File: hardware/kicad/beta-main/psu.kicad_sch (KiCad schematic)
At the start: 34 parts, among them J18 XT60, U5 AP3441SHE-7B, U6 TPS56624x, U7 AP2553W6

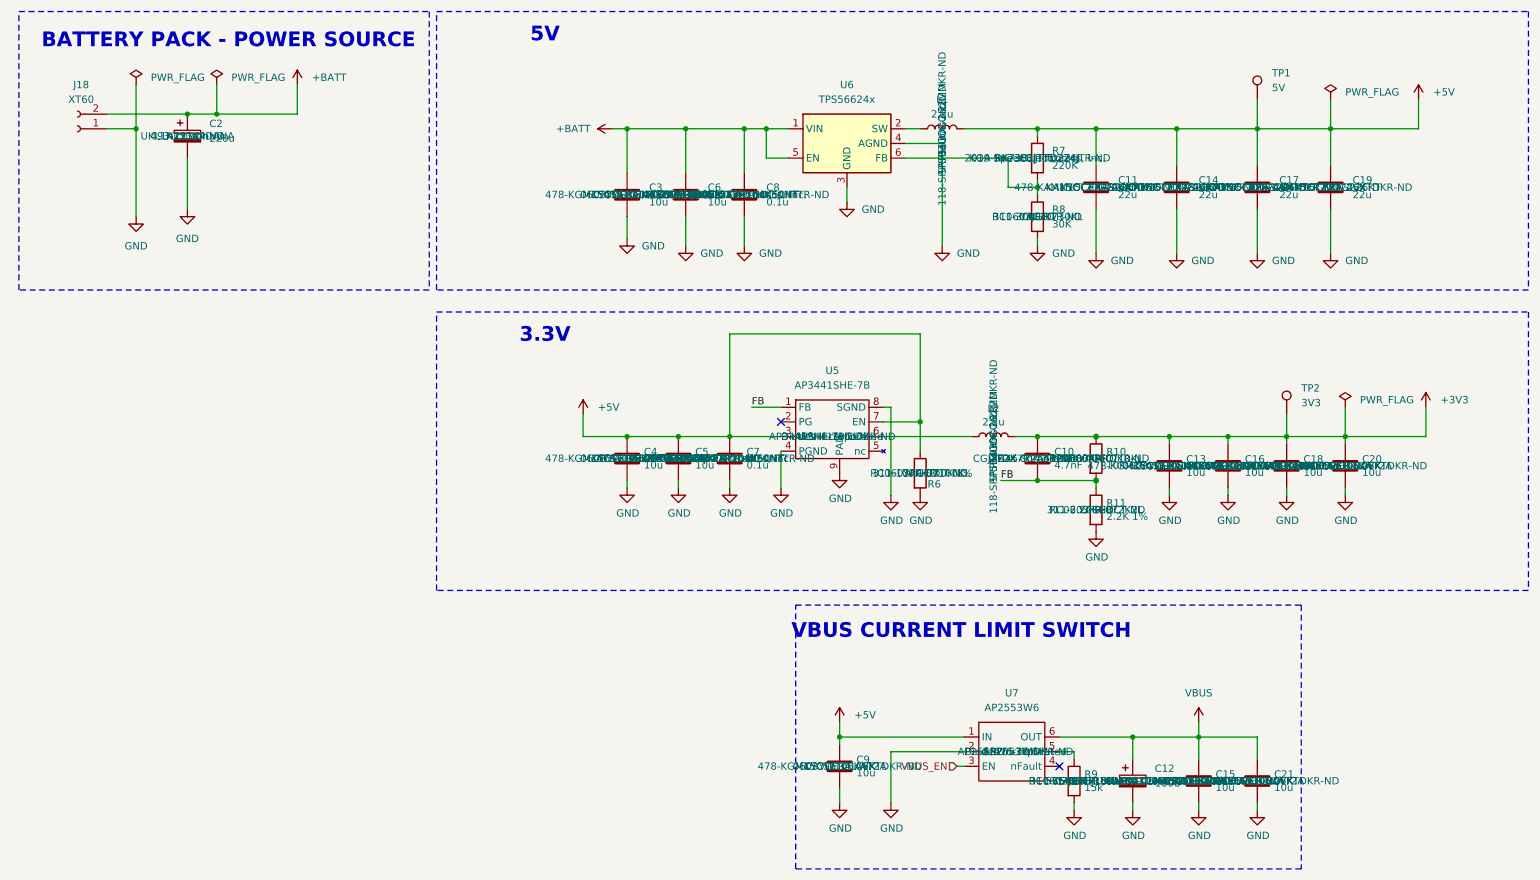
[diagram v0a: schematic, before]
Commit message: resolve DRC issues and generate fab files
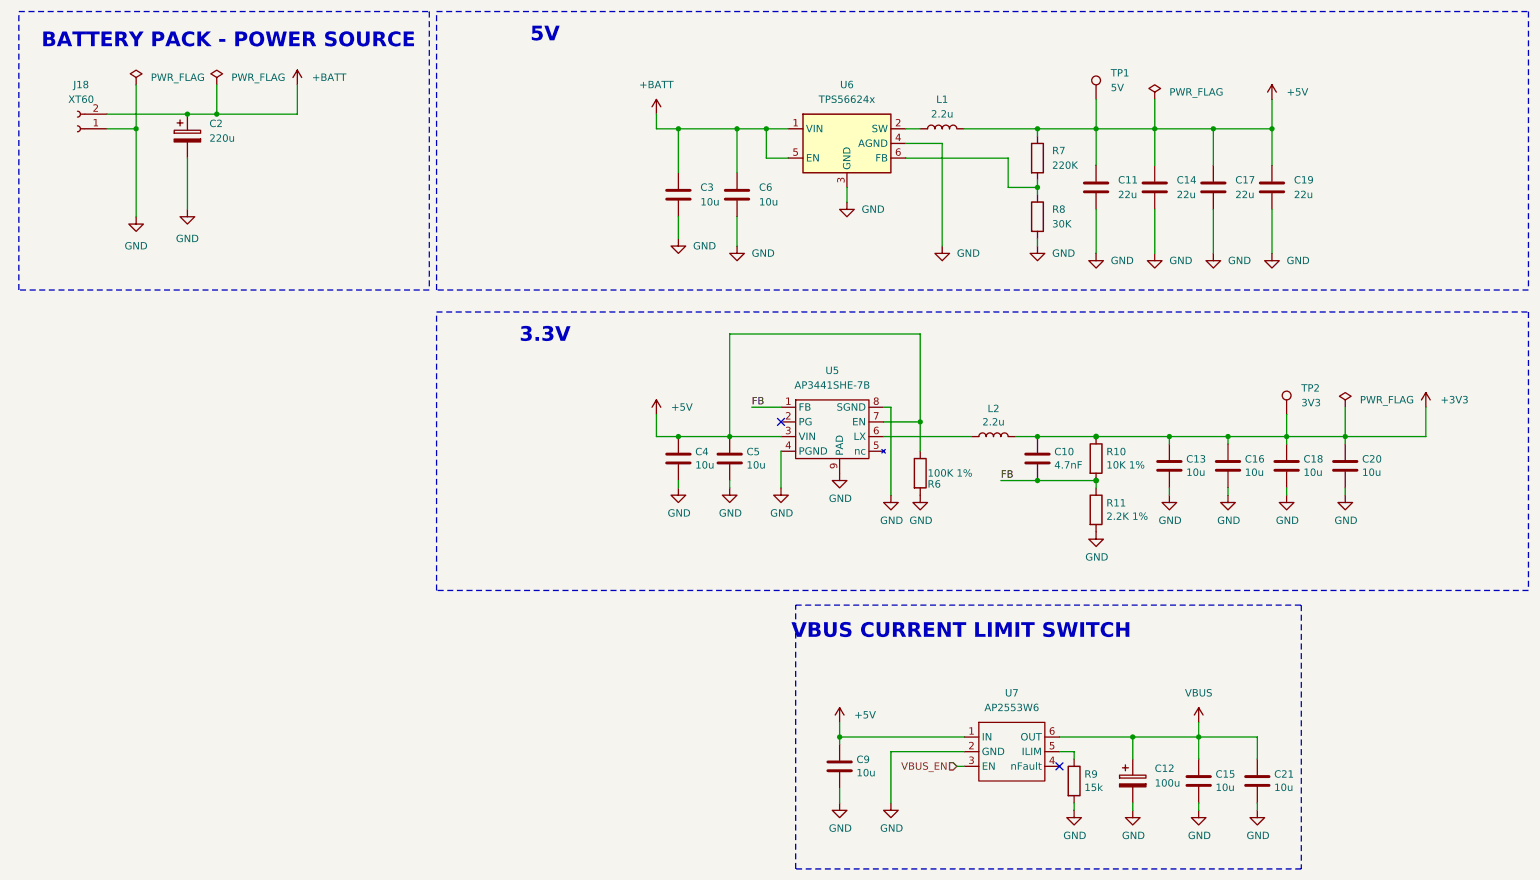
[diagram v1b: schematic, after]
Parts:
- removed C7, C8: 0.1u, Capacitor_SMD:C_0603_1608Metric, symbol Device:C
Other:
- moved on the sheet: C14, C17, C19, C3, C4, C5, C6, TP1

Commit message: add final touches, generate rev A fab and step files
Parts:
- removed C2: 220u, Capacitor_THT:CP_Radial_D8.0mm_P3.50mm, symbol Device:C_Polarized
- C11, C14, C17, C19: value 22u -> 10u
- C12: footprint Capacitor_SMD:CP_Elec_6.3x7.7 -> Capacitor_SMD:CP_Elec_6.3x5.7; MP EMHJ160ARA101MF80G -> RKS1E221MCNAHHGS
- R6: value 100K 1% -> 10k
- TP1, TP2: now left out of the parts list
